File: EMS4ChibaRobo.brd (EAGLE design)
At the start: 51 x 68 mm, 25 parts, among them CON1 XT60PB-F, CON2 XT60PB-M, CON3 XT60PB-M, CON4 XT60PB-M, CON5 XT60PB-M, IC1 7805DT, Q1 BUZ11BH, U9 XC6206

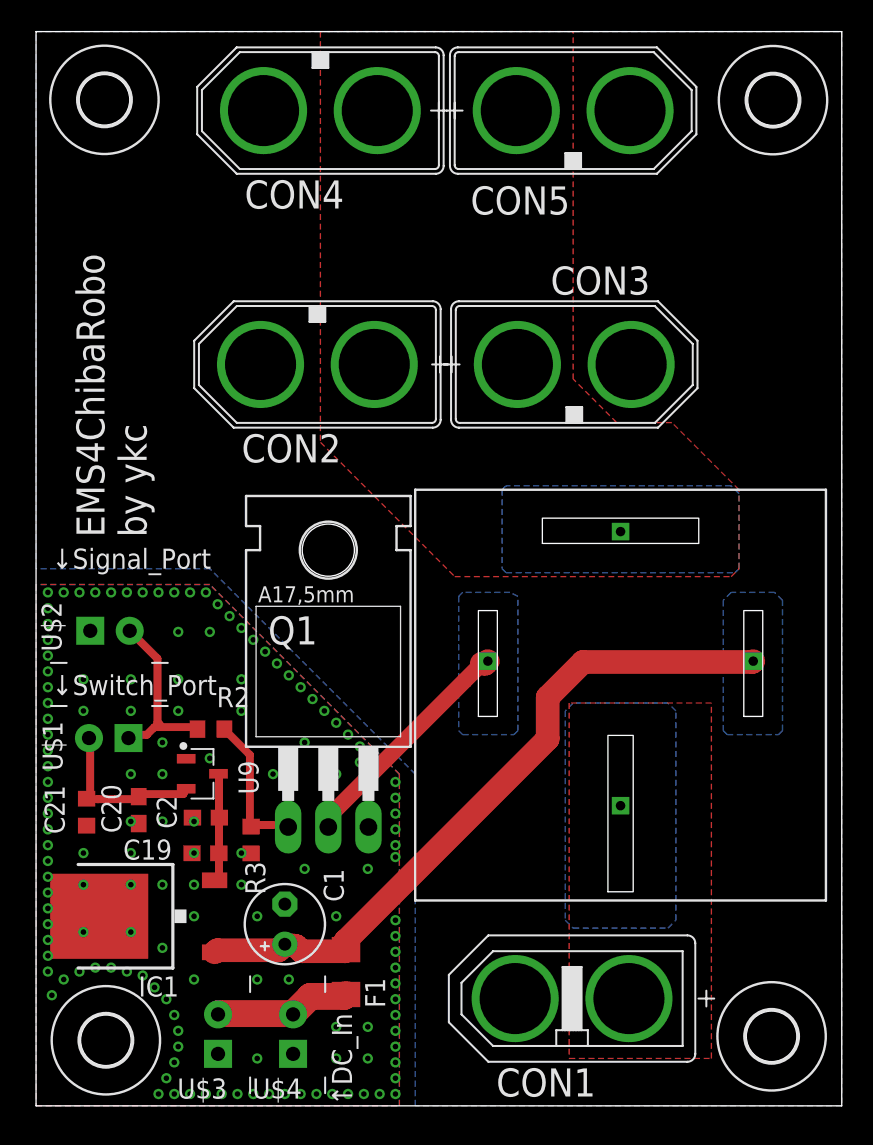
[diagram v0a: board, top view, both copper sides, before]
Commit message: 5V駆動に変更
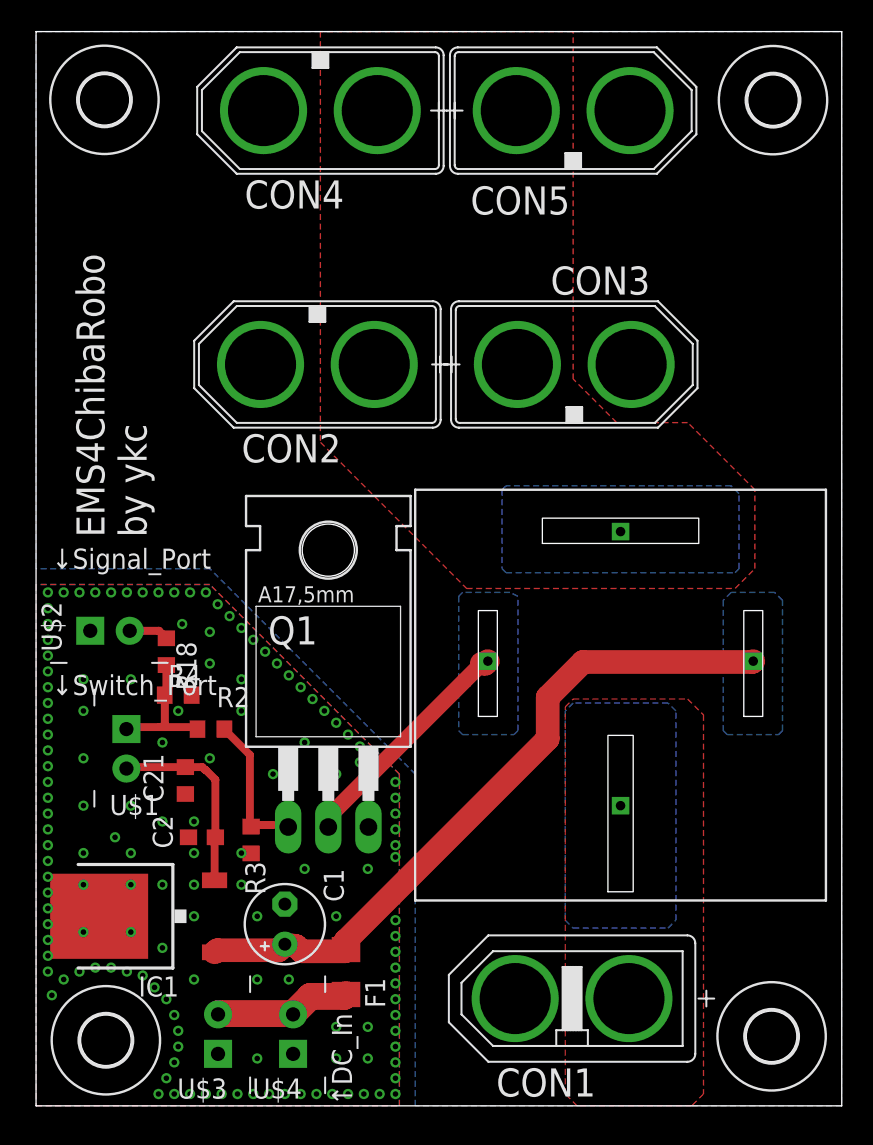
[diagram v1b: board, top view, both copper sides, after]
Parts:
- removed C19, C20: 1u, rcl:C0603
- removed U9: XC6206, torex:SOT95P240X110-3
- added R18: 1k, rcl:R0603
- added R4: 100k, rcl:R0603
- moved C21 6.56 mm to (9.45, 20.6)
- moved U$1 1.41 mm to (4.99, 22.6), turned to 90 degrees
- moved C2 1.27 mm to (10.5, 17.0)
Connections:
- removed net +3V3: C20.1, C21.2, U$1.P$2, U9.2
- new net !EMS1: R18.1, U$2.P$2
- net !EMS: now also R18.2, R4.1; no longer U$2.P$2
- net +5V: now also C21.2, U$1.P$2; no longer C19.1, U9.3
- net GNDIO: now also R4.2; no longer C19.2, C20.2, U9.1
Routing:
- net +3V3: track 10.5 -> 0.00 mm
- net +5V: track 6.98 -> 12.4 mm
- net !EMS: track 11.6 -> 8.71 mm
- net !EMS1: track 0.00 -> 2.51 mm

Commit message: Update Relay
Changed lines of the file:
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@@
 <contactref element="CON2" pad="-"/>
 <contactref element="CON3" pad="-"/>
-<polygon width="0.25" layer="16" pour="cutout">
-<vertex x="33.5" y="25"/>
-<vertex x="33.5" y="11.75"/>
-<vertex x="34" y="11.25"/>
-<vertex x="40" y="11.25"/>
-<vertex x="40.5" y="11.75"/>
-<vertex x="40.5" y="25"/>
-<vertex x="40" y="25.5"/>
-<vertex x="34" y="25.5"/>
-</polygon>
-<polygon width="0.508" layer="16" thermals="no">
+<contactref element="CON4" pad="-"/>
+<contactref element="CON5" pad="-"/>
+<polygon width="0.1524" layer="16" isolate="0.254">
+<vertex x="0" y="34"/>
+<vertex x="11" y="34"/>
+<vertex x="24" y="21"/>
+<vertex x="24" y="0"/>
+<vertex x="51" y="0"/>
 <vertex x="51" y="68"/>
-<vertex x="51" y="0"/>
-<vertex x="24" y="0"/>
-<vertex x="24" y="21"/>
-<vertex x="11" y="34"/>
-<vertex x="0" y="34"/>
 <vertex x="0" y="68"/>
 </polygon>
-<contactref element="CON4" pad="-"/>
-<contactref element="CON5" pad="-"/>
-<polygon width="0.25" layer="16" pour="cutout">
-<vertex x="26.75" y="32.25"/>
-<vertex x="26.75" y="23.75"/>
-<vertex x="27" y="23.5"/>
-<vertex x="30.25" y="23.5"/>
-<vertex x="30.5" y="23.75"/>
-<vertex x="30.5" y="32.25"/>
-<vertex x="30" y="32.5"/>
-<vertex x="27" y="32.5"/>
-</polygon>
-<polygon width="0.25" layer="16" pour="cutout">
-<vertex x="43.5" y="32"/>
-<vertex x="43.5" y="23.75"/>
-<vertex x="43.75" y="23.5"/>
-<vertex x="47" y="23.5"/>
-<vertex x="47.25" y="23.75"/>
-<vertex x="47.25" y="32"/>
-<vertex x="46.75" y="32.5"/>
-<vertex x="44" y="32.5"/>
-</polygon>
-<polygon width="0.25" layer="16" pour="cutout">
-<vertex x="29.75" y="33.75"/>
-<vertex x="44.25" y="33.75"/>
-<vertex x="44.5" y="34"/>
-<vertex x="44.5" y="38.75"/>
-<vertex x="44" y="39.25"/>
-<vertex x="29.75" y="39.25"/>
-<vertex x="29.5" y="39"/>
-<vertex x="29.5" y="34"/>
-</polygon>
+<wire x1="37.67" y1="46.93" x2="37.6" y2="63" width="0" layer="19" extent="1-1"/>
+<wire x1="14.4" y1="63" x2="37.6" y2="63" width="0" layer="19" extent="1-1"/>
+<wire x1="14.21" y1="46.93" x2="14.4" y2="63" width="0" layer="19" extent="1-1"/>
+<wire x1="30.33" y1="6.79" x2="37.67" y2="46.93" width="0" layer="19" extent="1-1"/>
 </signal>
 <signal name="BATT_POWER">

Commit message: シルクの調整
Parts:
- moved R2 2.15 mm to (9.32, 22.6)
- moved U$1 1.77 mm to (3.74, 21.4)
- moved C21 1.35 mm to (8.95, 19.3)
- moved R4 1.27 mm to (9.25, 24.8)
- moved C2 0.50 mm to (10.5, 16.5)
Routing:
- net !EMS: track 8.71 -> 9.48 mm
- net +12V: track 44.0 -> 44.6 mm

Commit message: update
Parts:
- removed S1: 897-1AH-C-001, relay:897-1AH-C-001
- added U$5: 897-1AH-C-001, CRS_EAGLE_Lib:897-1AH-C-001
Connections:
- net +12V: now also U$5.86_B, U$5.86_T; no longer S1.P$2
- net BATT_POWER: now also U$5.30_B, U$5.30_T; no longer S1.P$1
- net N$1: now also U$5.85_B, U$5.85_T; no longer S1.P$3
- net OUT_POWER_A: now also U$5.87_B, U$5.87_T; no longer S1.P$4
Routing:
- net +12V: track 44.6 -> 44.0 mm
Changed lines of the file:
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@@
 <drawing>
 <settings>
-<setting alwaysvectorfont="yes"/>
+<setting alwaysvectorfont="no"/>
 <setting verticaltext="up"/>
 </settings>
@@
 <attribute name="VALUE" x="38.5" y="58.7" size="1.778" layer="27" rot="R180"/>
 </element>
-<element name="S1" library="relay" package="897-1AH-C-001" value="897-1AH-C-001" x="37" y="26" smashed="yes"/>
 <element name="R18" library="rcl" library_urn="urn:adsk.eagle:library:334" package="R0603" package3d_urn="urn:adsk.eagle:package:23555/3" value="1k" x="8.25" y="28.75" smashed="yes" rot="R270">
 <attribute name="NAME" x="8.115" y="30.385" size="1.27" layer="25"/>
@@
 <attribute name="VALUE" x="8.615" y="22.845" size="1.27" layer="27"/>
 </element>
+<element name="U$5" library="CRS_EAGLE_Lib" package="897-1AH-C-001" value="897-1AH-C-001" x="37" y="25" smashed="yes"/>
 </elements>
 <signals>
@@
 <via x="22.75" y="9.75" extent="1-16" drill="0.35"/>
 <via x="22.75" y="8.75" extent="1-16" drill="0.35"/>
-<via x="22.75" y="20.5" extent="1-16" drill="0.35"/>
+<via x="16.75" y="20.5" extent="1-16" drill="0.35"/>
 <via x="22.75" y="19.5" extent="1-16" drill="0.35"/>
 <via x="22.75" y="18.5" extent="1-16" drill="0.35"/>
 <via x="22.75" y="17.5" extent="1-16" drill="0.35"/>
 <via x="22.75" y="16.5" extent="1-16" drill="0.35"/>
-<via x="20.5" y="21.75" extent="1-16" drill="0.35"/>
+<via x="19.5" y="21.75" extent="1-16" drill="0.35"/>
 <via x="20.5" y="22.75" extent="1-16" drill="0.35"/>
 <via x="19.75" y="23.5" extent="1-16" drill="0.35"/>
@@
 <via x="6" y="19" extent="1-16" drill="0.35"/>
 <via x="15" y="21" extent="1-16" drill="0.35"/>
-<via x="19" y="21" extent="1-16" drill="0.35"/>
+<via x="22.75" y="20.5" extent="1-16" drill="0.35"/>
 <via x="17" y="23" extent="1-16" drill="0.35"/>
 <via x="10" y="18" extent="1-16" drill="0.35"/>
@@
 <signal name="BATT_POWER">
 <contactref element="CON1" pad="+"/>
-<contactref element="S1" pad="P$1"/>
 <polygon width="0.508" layer="1" thermals="no">
 <vertex x="33.5" y="0.75"/>
@@
 <vertex x="34.25" y="0"/>
 </polygon>
+<contactref element="U$5" pad="30_B"/>
+<contactref element="U$5" pad="30_T"/>
+<wire x1="37" y1="17.5" x2="37" y2="17.5" width="0" layer="19" extent="1-16"/>
 </signal>
 <signal name="!EMS">
@@
 <vertex x="34" y="68"/>
 </polygon>
-<contactref element="S1" pad="P$4"/>
+<contactref element="U$5" pad="87_T"/>
+<contactref element="U$5" pad="87_B"/>
+<wire x1="37" y1="35.4" x2="37" y2="35.4" width="0" layer="19" extent="1-16"/>
 </signal>
 <signal name="+12V" class="1">
@@
 <wire x1="19.572" y1="9.786" x2="19.62" y2="9.892" width="1.5" layer="1"/>
 <wire x1="16.4731" y1="10.1122" x2="15.75" y2="10.23" width="1.5" layer="1"/>
-<wire x1="31.8888" y1="26.3648" x2="33.6213" y2="28.0973" width="1.5" layer="1"/>
-<wire x1="31.8888" y1="22.7338" x2="31.8888" y2="26.3648" width="1.5" layer="1"/>
+<wire x1="31.8888" y1="25.8648" x2="33.274" y2="27.25" width="1.5" layer="1"/>
+<wire x1="31.8888" y1="22.7338" x2="31.8888" y2="25.8648" width="1.5" layer="1"/>
 <wire x1="19.583690625" y1="10.428690625" x2="31.8888" y2="22.7338" width="1.5" layer="1"/>
 <wire x1="19.583690625" y1="10.428690625" x2="19.62" y2="9.892" width="1.5" layer="1"/>
-<contactref element="S1" pad="P$2"/>
-<wire x1="45.4" y1="28.15" x2="45.3473" y2="28.0973" width="1.5" layer="1"/>
-<wire x1="45.3473" y1="28.0973" x2="33.6213" y2="28.0973" width="1.5" layer="1"/>
+<contactref element="U$5" pad="86_T" route="any" routetag="G$1.1"/>
+<contactref element="U$5" pad="86_B" route="any" routetag="G$1.1"/>
+<wire x1="33.274" y1="27.25" x2="45.15" y2="27.25" width="1.5" layer="1"/>
+<wire x1="45.15" y1="27.25" x2="45.4" y2="27" width="1.5" layer="1"/>
 </signal>
 <signal name="+5V">
@@
 <wire x1="11.55645625" y1="5.8395" x2="11.52" y2="5.79" width="1.7" layer="1"/>
 </signal>
-<signal name="N$1">
-<contactref element="Q1" pad="D"/>
-<wire x1="18.5" y1="17.65" x2="18.4946" y2="17.6446" width="0.6096" layer="1"/>
-<wire x1="18.4946" y1="17.6446" x2="18.4946" y2="18.274775" width="0.6096" layer="1"/>
-<wire x1="28.209825" y1="27.99" x2="27.1099125" y2="26.8900875" width="1.016" layer="1"/>
-<contactref element="S1" pad="P$3"/>
-<wire x1="27.1099125" y1="26.8900875" x2="18.4946" y2="18.274775" width="1.016" layer="1"/>
-<wire x1="28.6" y1="28.15" x2="28.44" y2="27.99" width="1.5" layer="1"/>
-<wire x1="28.44" y1="27.99" x2="28.209825" y2="27.99" width="1.5" layer="1"/>
-</signal>
 <signal name="!EMS1">
 <contactref element="R18" pad="1"/>
@@
 <wire x1="7.78" y1="30.07" x2="8.25" y2="29.6" width="0.508" layer="1"/>
 </signal>
+<signal name="N$1">
+<contactref element="U$5" pad="85_T" route="any" routetag="G$1.2"/>
+<contactref element="U$5" pad="85_B" route="any" routetag="G$1.2"/>
+<contactref element="Q1" pad="D"/>
+<wire x1="27.09021875" y1="27" x2="18.2994" y2="18.20918125" width="1.5" layer="1"/>
+<wire x1="18.2994" y1="18.20918125" x2="18.2994" y2="17.8506" width="1.5" layer="1"/>
+<wire x1="18.5" y1="17.65" x2="18.2994" y2="17.8506" width="1.5" layer="1"/>
+<wire x1="28.6" y1="27" x2="27.09021875" y2="27" width="1.5" layer="1"/>
+</signal>
 </signals>
